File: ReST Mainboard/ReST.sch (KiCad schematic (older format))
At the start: 97 parts

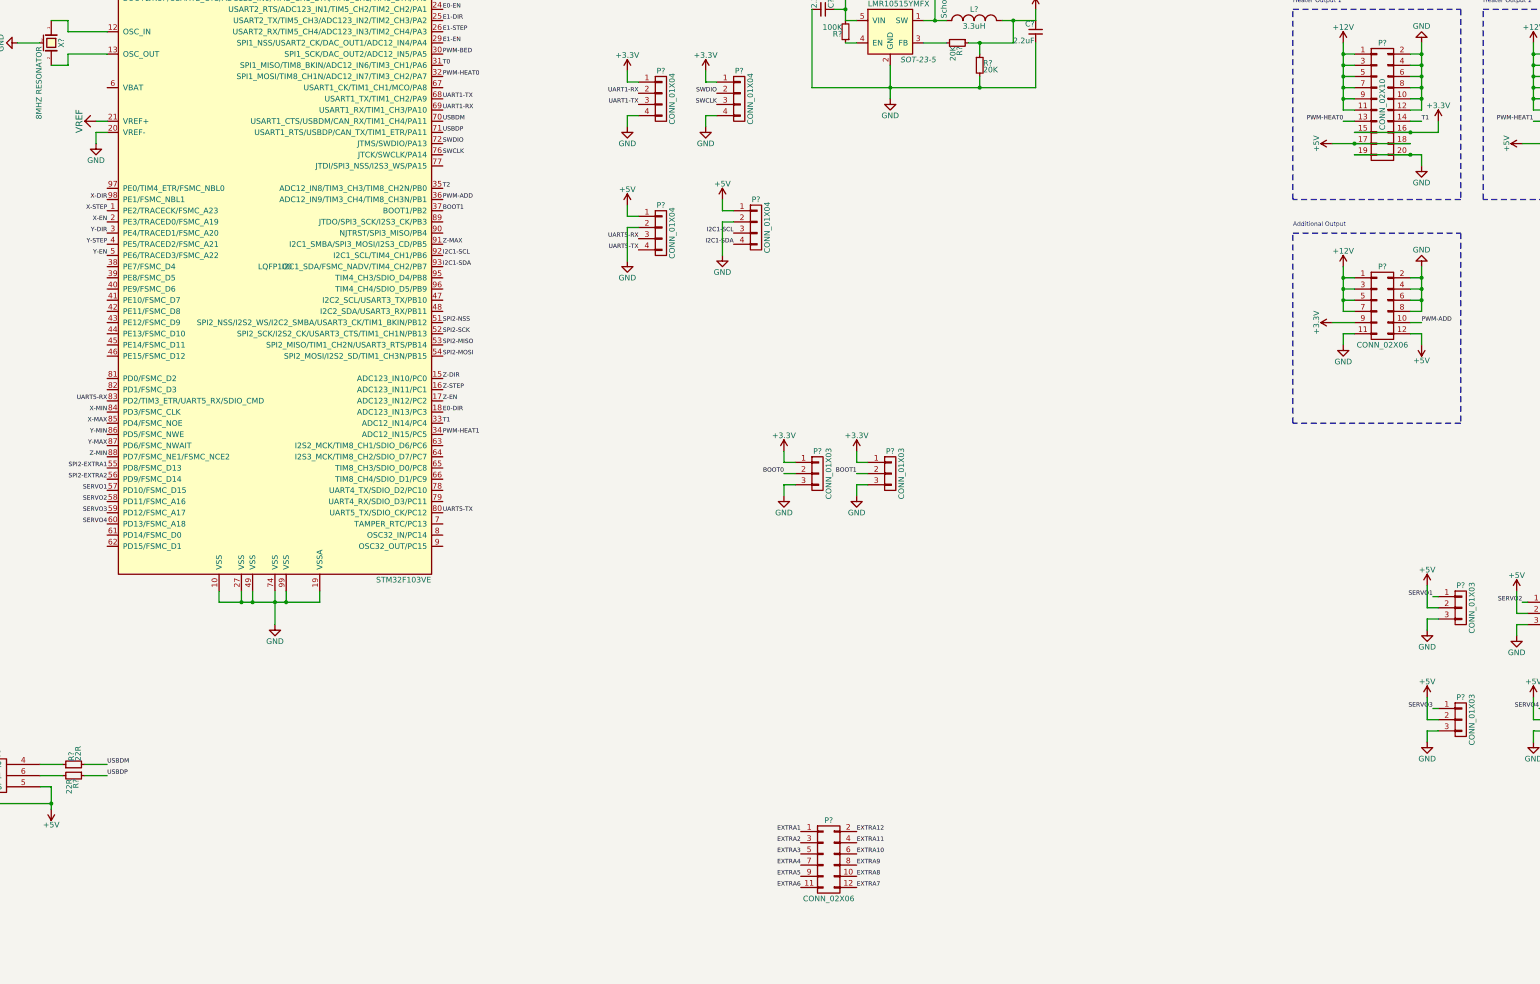
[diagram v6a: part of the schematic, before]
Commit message: Added Pin Def. on Mainboard + EEPROM
FInishing of for today: 
copied the pin def. of the mainboard and added a eeprom (AT24C128)
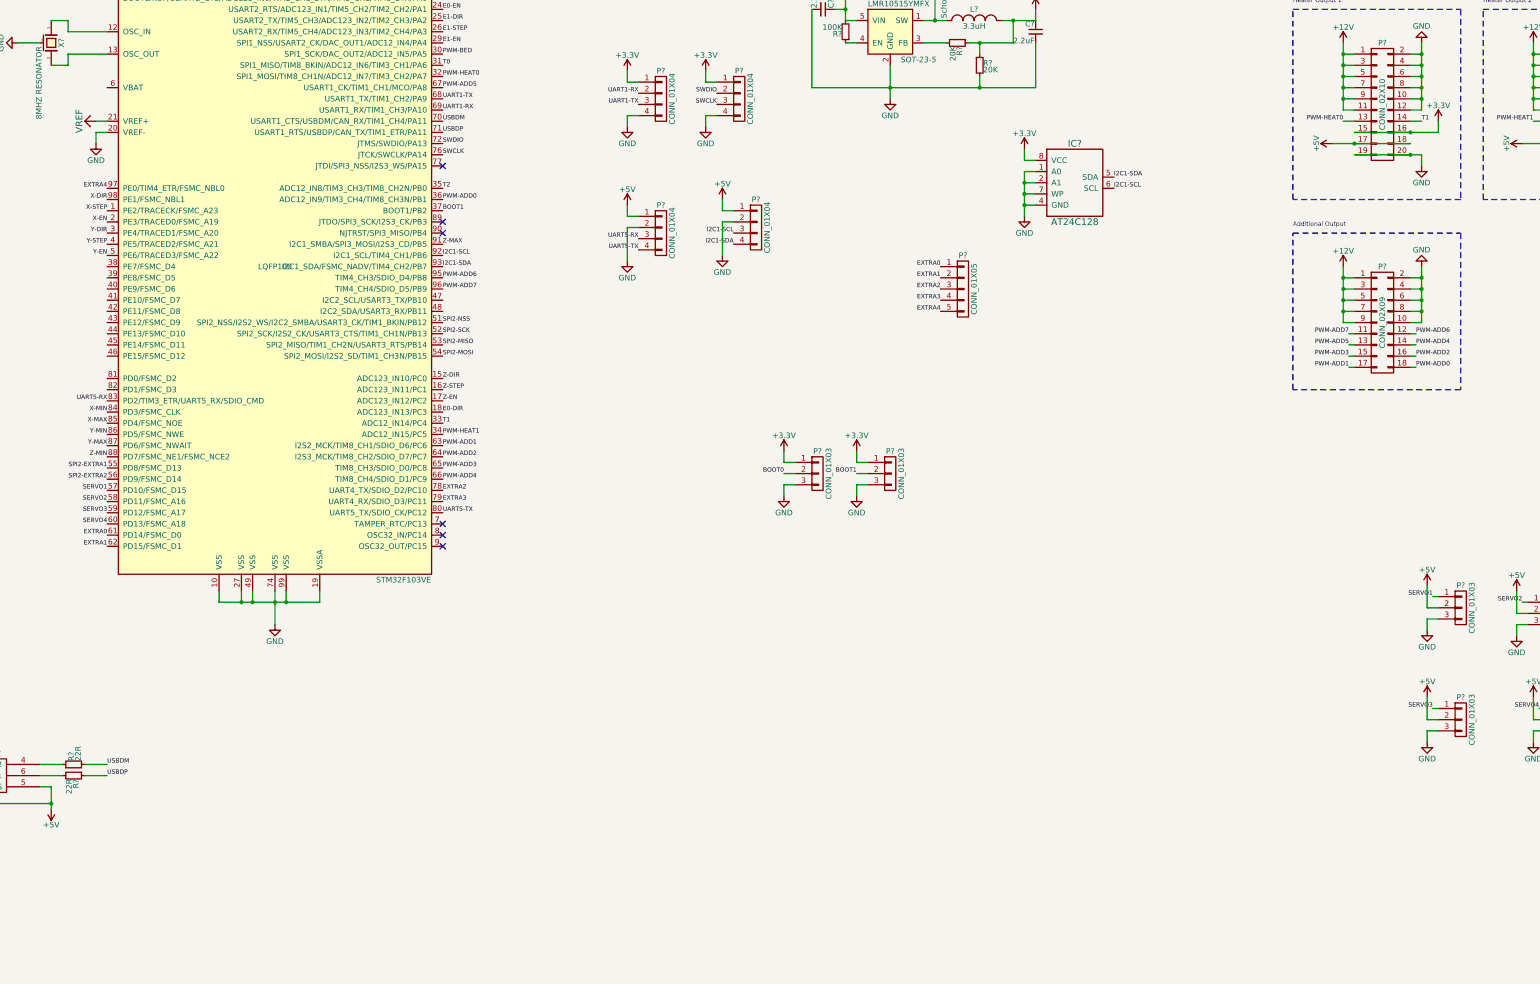
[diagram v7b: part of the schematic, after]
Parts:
- removed P? (x2): CONN_02X06, symbol CONN_02X06
- added IC?: AT24C128, symbol AT24C256
- added P?: CONN_02X09, symbol CONN_02X09
- added P?: CONN_01X05, symbol CONN_01X05
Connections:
- net +12V: now also P?.1 (P1), P?.3 (P3), P?.5 (P5), P?.7 (P7), P?.9 (P9)
- net +3V3: now also IC?.8 (VCC)
- net EXTRA1: now also U?.62 (PD15/FSMC_D1), P?.2 (P2)
- net EXTRA2: now also U?.78 (UART4_TX/SDIO_D2/PC10), P?.3 (P3)
- net EXTRA3: now also U?.79 (UART4_RX/SDIO_D3/PC11), P?.4 (P4)
- net EXTRA4: now also U?.97 (PE0/TIM4_ETR/FSMC_NBL0), P?.5 (P5)
- net GND: now also IC?.1 (A0), IC?.2 (A1), IC?.4 (GND), IC?.7 (WP), P?.10 (P10), P?.2 (P2), P?.4 (P4), P?.6 (P6), P?.8 (P8)
- net I2C1-SCL: now also IC?.6 (SCL)
- net I2C1-SDA: now also IC?.5 (SDA)
- net EXTRA0: now reaches U?.61 (PD14/FSMC_D0)
- net EXTRA0: now also P?.1 (P1)
- net PWM-ADD1: now reaches U?.63 (I2S2_MCK/TIM8_CH1/SDIO_D6/PC6)
- net PWM-ADD1: now also P?.17 (P17)
- net PWM-ADD2: now reaches U?.64 (I2S3_MCK/TIM8_CH2/SDIO_D7/PC7)
- net PWM-ADD2: now also P?.16 (P16)
- net PWM-ADD3: now reaches U?.65 (TIM8_CH3/SDIO_D0/PC8)
- net PWM-ADD3: now also P?.15 (P15)
- net PWM-ADD4: now reaches U?.66 (TIM8_CH4/SDIO_D1/PC9)
- net PWM-ADD4: now also P?.14 (P14)
- net PWM-ADD5: now reaches U?.67 (USART1_CK/TIM1_CH1/MCO/PA8)
- net PWM-ADD5: now also P?.13 (P13)
- net PWM-ADD6: now reaches U?.95 (TIM4_CH3/SDIO_D4/PB8)
- net PWM-ADD6: now also P?.12 (P12)
- net PWM-ADD7: now reaches U?.96 (TIM4_CH4/SDIO_D5/PB9)
- net PWM-ADD7: now also P?.11 (P11)
- net PWM-ADD renamed PWM-ADD0
- net PWM-ADD0: now also P?.18 (P18)
- no-connect marks 0 -> 6
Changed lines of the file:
@@
-$EndComp
-$Comp
-L +5V #PWR?
-U 1 1 56BC01ED
-P 15800 6900
-F 0 "#PWR?" H 15800 6750 50  0001 C CNN
-F 1 "+5V" H 15800 7040 50  0000 C CNN
-F 2 "" H 15800 6900 50  0000 C CNN
-F 3 "" H 15800 6900 50  0000 C CNN
-	1    15800 6900
-	-1   0    0    1
 $EndComp
 $Comp
@@
 	-1   0    0    1
 $EndComp
-$Comp
-L +3.3V #PWR?
-U 1 1 56BC01F9
-P 15000 6700
-F 0 "#PWR?" H 15000 6550 50  0001 C CNN
-F 1 "+3.3V" H 15000 6840 50  0000 C CNN
-F 2 "" H 15000 6700 50  0000 C CNN
-F 3 "" H 15000 6700 50  0000 C CNN
-	1    15000 6700
-	0    -1   -1   0
-$EndComp
-$Comp
-L GND #PWR?
-U 1 1 56BC0201
-P 15100 6900
-F 0 "#PWR?" H 15100 6650 50  0001 C CNN
-F 1 "GND" H 15100 6750 50  0000 C CNN
-F 2 "" H 15100 6900 50  0000 C CNN
-F 3 "" H 15100 6900 50  0000 C CNN
-	1    15100 6900
-	1    0    0    -1
-$EndComp
 Text Notes 14650 5850 0    39   ~ 0
 Additional Output
-$Comp
-L CONN_02X06 P?
-U 1 1 56BC0795
-P 15450 6550
-F 0 "P?" H 15450 6900 50  0000 C CNN
-F 1 "CONN_02X06" H 15450 6200 50  0000 C CNN
-F 2 "" H 15450 5350 50  0000 C CNN
-F 3 "" H 15450 5350 50  0000 C CNN
-	1    15450 6550
-	1    0    0    -1
-$EndComp
-Text Label 15800 6700 0    39   ~ 0
-PWM-ADD
 Wire Wire Line
 	3700 4400 3550 4400
@@
 	14650 5900 16150 5900
 Wire Notes Line
-	16150 5900 16150 7600
-Wire Notes Line
-	16150 7600 14650 7600
-Wire Notes Line
-	14650 7600 14650 5900
-Wire Wire Line
-	15100 6200 15100 6600
+	16150 7300 14650 7300
+Wire Wire Line
+	15100 6200 15100 6700
 Wire Wire Line
 	15100 6300 15200 6300
@@
 	15800 6600 15700 6600
 Wire Wire Line
-	15800 6200 15800 6600
+	15800 6200 15800 6700
 Wire Wire Line
 	15700 6300 15800 6300
@@
 	15700 6500 15800 6500
 Connection ~ 15800 6500
-Wire Wire Line
-	15800 6700 15700 6700
-Wire Wire Line
-	15700 6800 15800 6800
-Wire Wire Line
-	15800 6800 15800 6900
-Wire Wire Line
-	15000 6700 15200 6700
-Wire Wire Line
-	15200 6800 15100 6800
-Wire Wire Line
-	15100 6800 15100 6900
 Text Label 4050 5600 2    39   ~ 0
 X-DIR
@@
 T2
 Text Label 7050 5600 0    39   ~ 0
-PWM-ADD
+PWM-ADD0
 Text Label 4050 7500 2    39   ~ 0
 X-MIN
@@
 I2C1-SDA
 $Comp
-L CONN_02X06 P?
-U 1 1 56C08CB8
-P 10500 11500
-F 0 "P?" H 10500 11850 50  0000 C CNN
-F 1 "CONN_02X06" H 10500 11150 50  0000 C CNN
-F 2 "" H 10500 10300 50  0000 C CNN
-F 3 "" H 10500 10300 50  0000 C CNN
-	1    10500 11500
-	1    0    0    -1
-$EndComp
-Text Label 10250 11250 2    39   ~ 0
+L CONN_02X09 P?
+U 1 1 56C26034
+P 15450 6700
+F 0 "P?" H 15450 7200 50  0000 C CNN
+F 1 "CONN_02X09" V 15450 6700 50  0000 C CNN
+F 2 "" H 15450 5500 50  0000 C CNN
+F 3 "" H 15450 5500 50  0000 C CNN
+	1    15450 6700
+	1    0    0    -1
+$EndComp
+Wire Wire Line
+	15100 6700 15200 6700
+Connection ~ 15100 6600
+Wire Wire Line
+	15800 6700 15700 6700
+Connection ~ 15800 6600
+Wire Wire Line
+	15150 6800 15200 6800
+Wire Wire Line
+	15150 6900 15200 6900
+Wire Wire Line
+	15150 7000 15200 7000
+Wire Wire Line
+	15150 7100 15200 7100
+Wire Wire Line
+	15750 7100 15700 7100
+Wire Wire Line
+	15750 7000 15700 7000
+Wire Wire Line
+	15750 6900 15700 6900
+Wire Wire Line
+	15750 6800 15700 6800
+Wire Notes Line
+	16150 5900 16150 7300
+Wire Notes Line
+	14650 7300 14650 5900
+Text Label 15750 7100 0    39   ~ 0
+PWM-ADD0
+Text Label 15750 7000 0    39   ~ 0
+PWM-ADD2
+Text Label 15750 6900 0    39   ~ 0
+PWM-ADD4
+Text Label 15750 6800 0    39   ~ 0
+PWM-ADD6
+Text Label 15150 6800 2    39   ~ 0
+PWM-ADD7
+Text Label 15150 6900 2    39   ~ 0
+PWM-ADD5
+Text Label 15150 7000 2    39   ~ 0
+PWM-ADD3
+Text Label 15150 7100 2    39   ~ 0
+PWM-ADD1
+Text Label 7050 7800 0    39   ~ 0
+PWM-ADD1
+Text Label 7050 7900 0    39   ~ 0
+PWM-ADD2
+Text Label 7050 8000 0    39   ~ 0
+PWM-ADD3
+Text Label 7050 8100 0    39   ~ 0
+PWM-ADD4
+Text Label 7050 4600 0    39   ~ 0
+PWM-ADD5
+Text Label 4050 8600 2    39   ~ 0
+EXTRA0
+Text Label 4050 8700 2    39   ~ 0
 EXTRA1
-Text Label 10250 11350 2    39   ~ 0
+Text Label 7050 8200 0    39   ~ 0
 EXTRA2
-Text Label 10250 11450 2    39   ~ 0
+Text Label 7050 8300 0    39   ~ 0
 EXTRA3
-Text Label 10250 11550 2    39   ~ 0
+NoConn ~ 7050 8700
+NoConn ~ 7050 8600
+NoConn ~ 7050 8500
+Text Label 7050 6300 0    39   ~ 0
+PWM-ADD6
+Text Label 7050 6400 0    39   ~ 0
+PWM-ADD7
+Text Label 4050 5500 2    39   ~ 0
 EXTRA4
-Text Label 10250 11650 2    39   ~ 0
-EXTRA5
-Text Label 10250 11750 2    39   ~ 0
-EXTRA6
-Text Label 10750 11750 0    39   ~ 0
-EXTRA7
-Text Label 10750 11650 0    39   ~ 0
-EXTRA8
-Text Label 10750 11550 0    39   ~ 0
-EXTRA9
-Text Label 10750 11450 0    39   ~ 0
-EXTRA10
-Text Label 10750 11350 0    39   ~ 0
-EXTRA11
-Text Label 10750 11250 0    39   ~ 0
-EXTRA12
+NoConn ~ 7050 5300
+NoConn ~ 7050 5800
+NoConn ~ 7050 5900
+$Comp
+L CONN_01X05 P?
+U 1 1 56C38E8C
+P 11700 6400
+F 0 "P?" H 11700 6700 50  0000 C CNN
+F 1 "CONN_01X05" V 11800 6400 50  0000 C CNN
+F 2 "" H 11700 6400 50  0000 C CNN
+F 3 "" H 11700 6400 50  0000 C CNN
+	1    11700 6400
+	1    0    0    -1
+$EndComp
+Text Label 11500 6200 2    39   ~ 0
+EXTRA0
+Text Label 11500 6300 2    39   ~ 0
+EXTRA1
+Text Label 11500 6400 2    39   ~ 0
+EXTRA2
+Text Label 11500 6500 2    39   ~ 0
+EXTRA3
+Text Label 11500 6600 2    39   ~ 0
+EXTRA4
+$Comp
+L AT24C256 IC?
+U 1 1 56C3AD82
+P 12700 5450
+F 0 "IC?" H 12700 5800 60  0000 C CNN
+F 1 "AT24C128" H 12700 5100 60  0000 C CNN
+F 2 "" H 12700 5450 60  0000 C CNN
+F 3 "" H 12700 5450 60  0000 C CNN
+	1    12700 5450
+	1    0    0    -1
+$EndComp
+$Comp
+L +3.3V #PWR?
+U 1 1 56C3D723
+P 12250 5150
+F 0 "#PWR?" H 12250 5000 50  0001 C CNN
+F 1 "+3.3V" H 12250 5290 50  0000 C CNN
+F 2 "" H 12250 5150 50  0000 C CNN
+F 3 "" H 12250 5150 50  0000 C CNN
+	1    12250 5150
+	1    0    0    -1
+$EndComp
+Wire Wire Line
+	12350 5250 12250 5250
+Wire Wire Line
+	12250 5250 12250 5150
+$Comp
+L GND #PWR?
+U 1 1 56C3DB7C
+P 12250 5750
+F 0 "#PWR?" H 12250 5500 50  0001 C CNN
+F 1 "GND" H 12250 5600 50  0000 C CNN
+F 2 "" H 12250 5750 50  0000 C CNN
+F 3 "" H 12250 5750 50  0000 C CNN
+	1    12250 5750
+	1    0    0    -1
+$EndComp
+Wire Wire Line
+	12250 5350 12250 5750
+Wire Wire Line
+	12250 5650 12350 5650
+Text Label 13050 5500 0    39   ~ 0
+I2C1-SCL
+Text Label 13050 5400 0    39   ~ 0
+I2C1-SDA
+Wire Wire Line
+	12350 5550 12250 5550
+Connection ~ 12250 5650
+Wire Wire Line
+	12350 5450 12250 5450
+Connection ~ 12250 5550
+Wire Wire Line
+	12350 5350 12250 5350
+Connection ~ 12250 5450
 $EndSCHEMATC

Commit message: Final Version of Main Controller Schematic
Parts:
- removed C?: 4.7uF, symbol C_Small
- removed C? (x2): 2.2uF, symbol C_Small
- removed D?: Schottky TBD, symbol D_Schottky_Small
- removed L?: 3.3uH, symbol INDUCTOR_SMALL
- removed P?: SCREW_01X03, symbol CONN_01X03
- removed P?: CONN_01X03, symbol CONN_01X03
- removed P? (x4): CONN_01X04, symbol CONN_01X04
- removed P?: CONN_02X09, symbol CONN_02X09
- removed P?: CONN_01X05, symbol CONN_01X05
- removed R? (x2): 100K, symbol R_Small
- removed R? (x2): 20K, symbol R_Small
- removed U?: LM7805, symbol LM7805
- removed U?: LMR10515YMFX, SOT-23-5, symbol LMR10510YMF
- added C12: 22uF, ok-polcaps-panasonic:CP-PANASONIC-SMT_D, symbol C_Small
- added C13: 220uF, ok-polcaps-panasonic:CP-PANASONIC-SMT_D, symbol C_Small
- added C25: 100uF, symbol CP1_Small
- added C3: 100nF, ok-smd-generic:0805, symbol C_Small
- added D1: 1N5819, DO-214AC(SMA):DO-214AC(SMA), symbol D_Schottky_Small
- added L2: 330uH, Inductors:SELF-WE-PD-XXL, symbol INDUCTOR_SMALL
- added P10: CONN_01X04, symbol CONN_01X04
- added P15: CONN_02X07, Pin_Headers:Pin_Header_Angled_2x07, symbol CONN_02X07
- added P3, P9: CONN_01X04, Pin_Headers:Pin_Header_Straight_1x04, symbol CONN_01X04
- added P40: SCREW_01X04, symbol CONN_01X04
- added P46: CONN_02X04, symbol CONN_02X04
- added P52: CONN_02X03, symbol CONN_02X03
- added P53: CONN_02X07, Pin_Headers:Pin_Header_Straight_2x07, symbol CONN_02X07
- added P6: CONN_01X05, Pin_Headers:Pin_Header_Straight_1x05, symbol CONN_01X05
- added P7, P8: CONN_02X05, symbol CONN_02X05
- added P?: CONN_01X03, Pin_Headers:Pin_Header_Straight_1x03, symbol CONN_01X03
- added R1: 1M, symbol R_Small
- added R13: 100K, symbol R_Small
- added R4: 47R, ok-smd-generic:0805, symbol R_Small
- added R5: 10K, ok-smd-generic:0805, symbol R_Small
- added R6: 2K7, ok-smd-generic:0805, symbol R_Small
- added R7: 1K6, ok-smd-generic:0805, symbol R_Small
- added SW1: SW-SPST-NO, Buttons_Switches_ThroughHole:SW_PUSH_SMALL, symbol SW-SPST-NO
- added U10: POLOLU_A4988, symbol POLOLU_A4988
- added U3: L7805ACD2T-TR, TO_SOT_Packages_SMD:SOT-404, symbol LM117H
- added U4: LM2574N-ADJ, DIP-8, symbol LM2574N-ADJ
- C10, C8: renamed from C?; value 1uF -> 10uF; footprint (none) -> ok-polcaps-panasonic:CP-PANASONIC-SMT_C
- C11: renamed from C?; value 100nF -> 22uF; footprint (none) -> ok-polcaps-panasonic:CP-PANASONIC-SMT_D
- C2, C4, C5, C6, C7, C9: renamed from C?; footprint (none) -> ok-smd-generic:0805
- L1: renamed from L?; value INDUCTOR_SMALL -> BEAD; footprint (none) -> ok-smd-generic:1206
- P12, P16: renamed from P?; footprint (none) -> Pin_Headers:Pin_Header_Straight_2x04
- P13: renamed from P?; footprint (none) -> Pin_Headers:Pin_Header_Angled_2x04
- P14, P21: renamed from P?; footprint (none) -> Pin_Headers:Pin_Header_Angled_2x10
- P24, P26, P28, P30, P32, P34, P4, P5: renamed from P?; footprint (none) -> Pin_Headers:Pin_Header_Straight_1x03
- gave numbers to parts that had none: 56
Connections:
- net PWM-ADD4 is gone; now on net EXTRA2: U2.66 (TIM8_CH4/SDIO_D1/PC9)
- net PWM-ADD5 is gone; now on net EXTRA3: U2.67 (USART1_CK/TIM1_CH1/MCO/PA8)
- net PWM-ADD6 is gone; now on net X-DIR: U2.95 (TIM4_CH3/SDIO_D4/PB8)
- net PWM-ADD7 is gone; now on net X-STEP: U2.96 (TIM4_CH4/SDIO_D5/PB9)
- net VDD is gone; now on net +5V: C11.2
- net +12V: now also C12.1, C25.1, P15.1 (P1), P15.3 (P3), P15.5 (P5), P15.7 (P7), P15.9 (P9), U10.8 (VMOT), U3.1 (IN), U4.5 (VIN)
- net +3V3: now also C13.1, L2.2, P52.2 (P2), P52.4 (P4), P52.6 (P6), P53.13 (P13), P6.2 (P2), P7.4 (P4), P?.3 (P3), R5.2, R6.1, U10.2 (VDD)
- net +5V: now also P10.1 (P1), P3.1 (P1), P53.14 (P14), P6.5 (P5), P7.2 (P2), P9.1 (P1), P?.1 (P1), U3.3 (OUT); no longer C1.1, U1.5 (VBUS)
- net E0-DIR: now also U2.15 (ADC123_IN10/PC0); no longer U2.18 (ADC123_IN13/PC3)
- net E0-EN: now also U2.17 (ADC123_IN12/PC2); no longer U2.24 (USART2_RTS/ADC123_IN1/TIM5_CH2/TIM2_CH2/PA1)
- net E0-STEP: now also U2.16 (ADC123_IN11/PC1); no longer U2.23 (WKUP/USART2_CTS/ADC123_IN0/TIM2_CH1_ETR/TIM5_CH1/TIM8_ETR/PA0)
- net E1-DIR: now also U2.18 (ADC123_IN13/PC3); no longer U2.25 (USART2_TX/TIM5_CH3/ADC123_IN2/TIM2_CH3/PA2)
- net E1-EN: now also U2.24 (USART2_RTS/ADC123_IN1/TIM5_CH2/TIM2_CH2/PA1); no longer U2.29 (SPI1_NSS/USART2_CK/DAC_OUT1/ADC12_IN4/PA4)
- net E1-STEP: now also U2.23 (WKUP/USART2_CTS/ADC123_IN0/TIM2_CH1_ETR/TIM5_CH1/TIM8_ETR/PA0); no longer U2.26 (USART2_RX/TIM5_CH4/ADC123_IN3/TIM2_CH4/PA3)
- net ENDSTOP_VCC: now also P?.2 (P2)
- net EXTRA0: now also P53.2 (P2)
- net EXTRA1: now also P53.4 (P4)
- net EXTRA2: now also P53.6 (P6); no longer U2.78 (UART4_TX/SDIO_D2/PC10)
- net EXTRA3: now also P53.8 (P8); no longer U2.79 (UART4_RX/SDIO_D3/PC11)
- net EXTRA4: now also U2.78 (UART4_TX/SDIO_D2/PC10), P53.10 (P10); no longer U2.97 (PE0/TIM4_ETR/FSMC_NBL0)
- net GND: now also C12.2, C13.2, C25.2, C3.1, D1.2 (A), P10.4 (P4), P15.10 (P10), P15.2 (P2), P15.4 (P4), P15.6 (P6), P15.8 (P8), P3.3 (P3), P53.1 (P1), P53.11 (P11), P53.3 (P3), P53.5 (P5), P53.7 (P7), P53.9 (P9), P6.1 (P1), P7.1 (P1), P9.2 (P2), R1.1, R13.2, R7.2, SW1.1, U10.1 (GND), U10.7 (GND), U3.2 (GND), U4.3 (SGND), U4.4 (PGND)
- net PWM-ADD0: now also P15.14 (P14)
- net PWM-ADD1: now also P15.13 (P13)
- net PWM-ADD2: now also P15.12 (P12)
- net PWM-ADD3: now also P15.11 (P11)
- net SWCLK: now also P3.2 (P2)
- net SWDIO: now also P3.4 (P4)
- net UART1-RX: now also P10.3 (P3)
- net UART1-TX: now also P10.2 (P2)
- net UART5-RX: now also P9.3 (P3)
- net UART5-TX: now also P9.4 (P4)
- net VCC: now also C1.1, U1.5 (VBUS)
- net VREF: now also R4.2; no longer U2.21 (VREF+)
- net X-DIR: no longer U2.98 (PE1/FSMC_NBL1)
- net X-EN: now also U2.97 (PE0/TIM4_ETR/FSMC_NBL0); no longer U2.2 (PE3/TRACED0/FSMC_A19)
- net X-STEP: no longer U2.1 (PE2/TRACECK/FSMC_A23)
- net Y-DIR: now also U2.98 (PE1/FSMC_NBL1); no longer U2.3 (PE4/TRACED1/FSMC_A20)
- net Y-EN: now also U2.2 (PE3/TRACED0/FSMC_A19); no longer U2.5 (PE6/TRACED3/FSMC_A22)
- net Y-STEP: now also U2.1 (PE2/TRACECK/FSMC_A23); no longer U2.4 (PE5/TRACED2/FSMC_A21)
- net Z-DIR: now also U2.3 (PE4/TRACED1/FSMC_A20); no longer U2.15 (ADC123_IN10/PC0)
- net Z-EN: now also U2.5 (PE6/TRACED3/FSMC_A22); no longer U2.17 (ADC123_IN12/PC2)
- net Z-STEP: now also U2.4 (PE5/TRACED2/FSMC_A21); no longer U2.16 (ADC123_IN11/PC1)
- net at U2.14 (~NRST): now also C3.2, R5.1, SW1.2
- net LCD-D0: now reaches U2.38 (PE7/FSMC_D4)
- net LCD-D0: now also P8.10 (P10)
- net LCD-D1: now reaches U2.39 (PE8/FSMC_D5)
- net LCD-D1: now also P8.9 (P9)
- net LCD-D2: now reaches U2.40 (PE9/FSMC_D6)
- net LCD-D2: now also P8.8 (P8)
- net LCD-D3: now reaches U2.41 (PE10/FSMC_D7)
- net LCD-D3: now also P8.7 (P7)
- net LCD-D4: now reaches U2.42 (PE11/FSMC_D8)
- net LCD-D4: now also P8.6 (P6)
- net LCD-D5: now reaches U2.43 (PE12/FSMC_D9)
- net LCD-D5: now also P8.5 (P5)
- net LCD-D6: now reaches U2.44 (PE13/FSMC_D10)
- net LCD-D6: now also P8.4 (P4)
- net LCD-D7: now reaches U2.45 (PE14/FSMC_D11)
- net LCD-D7: now also P8.3 (P3)
- net LCD-CS: now reaches U2.46 (PE15/FSMC_D12)
- net LCD-CS: now also P8.2 (P2)
- net LCD-CD: now reaches U2.47 (I2C2_SCL/USART3_TX/PB10)
- net LCD-CD: now also P8.1 (P1)
- net LCD-WR: now reaches U2.48 (I2C2_SDA/USART3_RX/PB11)
- net LCD-WR: now also P7.9 (P9)
- net at P1.6 (shield): now also R1.2
- net I2C1-SCL renamed I2C-SCL
- net I2C-SCL: now also P6.3 (P3)
- net I2C1-SDA renamed I2C-SDA
- net I2C-SDA: now also P6.4 (P4)
- net SPI2-EXTRA1 renamed SPI-CS2
- net SPI-CS2: now also P7.8 (P8)
- net SPI2-EXTRA2 renamed LCD-RD
- net LCD-RD: now also P7.10 (P10)
- net SPI2-MISO renamed SPI-MISO
- net SPI-MISO: now also P7.5 (P5)
- net SPI2-MOSI renamed SPI-MOSI
- net SPI-MOSI: now also P7.7 (P7)
- net SPI2-NSS renamed SPI-CS1
- net SPI-CS1: now also P7.6 (P6)
- net SPI2-SCK renamed SPI-SCK
- net SPI-SCK: now also P7.3 (P3)
- new net: R4.1, U2.21 (VREF+)
- new net: R6.2, R7.1, U4.1 (FB)
- new net: D1.1 (K), L2.1, U4.7 (OUT)
- new net: P52.5 (P5), R13.1, U10.10 (MS1)
- new net: P52.3 (P3), U10.11 (MS2)
- new net: P52.1 (P1), U10.12 (MS3)
- new net: U10.13 (RST), U10.14 (SLP)
- new net: P46.2 (P2), U10.3 (IB)
- new net: P46.4 (P4), U10.4 (1A)
- new net: P46.6 (P6), U10.5 (2A)
- new net: P46.8 (P8), U10.6 (2B)
- new net: P40.4 (P4), P46.1 (P1)
- new net: P40.3 (P3), P46.3 (P3)
- new net: P40.2 (P2), P46.5 (P5)
- new net: P40.1 (P1), P46.7 (P7)
- new net E2-DIR: U10.16 (DIR), U2.25 (USART2_TX/TIM5_CH3/ADC123_IN2/TIM2_CH3/PA2)
- new net E2-EN: U10.9 (EN), U2.29 (SPI1_NSS/USART2_CK/DAC_OUT1/ADC12_IN4/PA4)
- new net E2-STEP: U10.15 (STEP), U2.26 (USART2_RX/TIM5_CH4/ADC123_IN3/TIM2_CH4/PA3)
- new net EXTRA5: P53.12 (P12), U2.79 (UART4_RX/SDIO_D3/PC11)
- no-connect marks 6 -> 10
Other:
- note added: "12/24V -> 5V REGULATOR"
- note added: "BOOT SELECT"
- note added: "EEPROM"
- note added: "EXTRA-PINHEADER"
- note added: "I2C CONNECTOR"
- note added: "Idea: Usage of 8080 full color \nLCD with Touch & SD Support\n(Custom?)"
- note added: "LCD CONNECTOR"
- note added: "PWR-IN"
- note added: "SERVO"
- note added: "SPI/LCD CONNECTOR"
- note added: "SWD"
- note added: "UART CONNECTOR"
- note added: "VIN -> 3.3V BUCK CONVERTER"
- note removed: "VCC: 5V over USB\nVDD: 5V over LDO (12V Rail)"
- moved on the sheet: C1, F1, IC1, P2
